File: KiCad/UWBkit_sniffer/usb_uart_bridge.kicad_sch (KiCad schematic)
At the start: 0 parts

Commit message: Added components to schematic
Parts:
- added C11: 100n, Capacitor_SMD:C_0603_1608Metric, symbol Device:C_Small
- added C12: 1u, Capacitor_Tantalum_SMD:CP_EIA-3216-18_Kemet-A, symbol Device:C_Polarized_Small
- added D6: G, LED_SMD:LED_0603_1608Metric, symbol Device:LED_Small
- added D7: R, LED_SMD:LED_0603_1608Metric, symbol Device:LED_Small
- added R10: 24k, Resistor_SMD:R_0603_1608Metric, symbol Device:R_Small
- added R11: 47k, Resistor_SMD:R_0603_1608Metric, symbol Device:R_Small
- added R13: 2k1, Resistor_SMD:R_0603_1608Metric, symbol Device:R_Small
- added R14: 3k3, Resistor_SMD:R_0603_1608Metric, symbol Device:R_Small
- added U2: CP2104, Package_DFN_QFN:QFN-24-1EP_4x4mm_P0.5mm_EP2.6x2.6mm, symbol Interface_USB:CP2104
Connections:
- new net: R10.2, R11.1, U2.8 (VBUS)
- new net: D6.1 (K), R13.1
- new net: R13.2, U2.13 (RXT/GPIO.1)
- new net: R14.1, U2.14 (TXT/GPIO.0)
- new net: D7.1 (K), R14.2
- new net +3V3: C11.1, C12.1, D6.2 (A), D7.2 (A), U2.5 (VIO), U2.6 (VDD), U2.7 (REGIN)
- new net D+: U2.3 (D+)
- new net D-: U2.4 (D-)
- new net GND: C11.2, C12.2, R11.2, U2.2 (GND), U2.25 (GND)
- new net RXD: U2.20 (RXD)
- new net TXD: U2.21 (TXD)
- new net VBUS: R10.1
- new net nRST: U2.9 (~{RST})
- no-connect marks 0 -> 11
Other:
- note added: "RX LED"
- note added: "TX LED"

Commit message: First version of PCB
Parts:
- added J11: Conn_01x02, Connector_PinHeader_2.54mm:PinHeader_1x02_P2.54mm_Vertical, symbol Connector_Generic:Conn_01x02
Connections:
- net RXD: now also J11.2 (Pin_2)
- net TXD: now also J11.1 (Pin_1)
- net at U2.14 (TXT/GPIO.0): now also R14.2; no longer R14.1
- net at D7.1 (K): now also R14.1; no longer R14.2
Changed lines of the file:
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@@
+	)
+	(junction
+		(at 166.37 72.39)
+		(diameter 0)
+		(color 0 0 0 0)
 	)
 	(junction
@@
 		(color 0 0 0 0)
 	)
+	(junction
+		(at 166.37 69.85)
+		(diameter 0)
+		(color 0 0 0 0)
+	)
 	(no_connect
 		(at 161.29 80.01)
@@
 	(wire
 		(pts
+			(xy 172.72 76.2) (xy 166.37 76.2)
+		)
+		(stroke
+			(width 0)
+			(type default)
+		)
+	)
+	(wire
+		(pts
+			(xy 166.37 72.39) (xy 168.91 72.39)
+		)
+		(stroke
+			(width 0)
+			(type default)
+		)
+	)
+	(wire
+		(pts
 			(xy 146.05 62.23) (xy 148.59 62.23)
 		)
@@
 	(wire
 		(pts
+			(xy 172.72 66.04) (xy 166.37 66.04)
+		)
+		(stroke
+			(width 0)
+			(type default)
+		)
+	)
+	(wire
+		(pts
 			(xy 102.87 69.85) (xy 102.87 71.12)
 		)
@@
 	(wire
 		(pts
-			(xy 161.29 69.85) (xy 163.83 69.85)
+			(xy 161.29 69.85) (xy 166.37 69.85)
 		)
 		(stroke
@@
 	(wire
 		(pts
+			(xy 166.37 69.85) (xy 168.91 69.85)
+		)
+		(stroke
+			(width 0)
+			(type default)
+		)
+	)
+	(wire
+		(pts
 			(xy 105.41 68.58) (xy 105.41 69.85)
 		)
@@
 	(wire
 		(pts
+			(xy 166.37 76.2) (xy 166.37 72.39)
+		)
+		(stroke
+			(width 0)
+			(type default)
+		)
+	)
+	(wire
+		(pts
 			(xy 173.99 106.68) (xy 172.72 106.68)
 		)
@@
 	(wire
 		(pts
-			(xy 161.29 72.39) (xy 163.83 72.39)
+			(xy 166.37 66.04) (xy 166.37 69.85)
+		)
+		(stroke
+			(width 0)
+			(type default)
+		)
+	)
+	(wire
+		(pts
+			(xy 161.29 72.39) (xy 166.37 72.39)
 		)
 		(stroke
@@
 		)
 	)
+	(hierarchical_label "RXD"
+		(shape input)
+		(at 172.72 76.2 0)
+		(effects
+			(font
+				(size 1.27 1.27)
+			)
+			(justify left)
+		)
+	)
 	(hierarchical_label "VBUS"
 		(shape input)
@@
 		)
 	)
-	(hierarchical_label "RXD"
-		(shape input)
-		(at 163.83 72.39 0)
-		(effects
-			(font
-				(size 1.27 1.27)
-			)
-			(justify left)
-		)
-	)
 	(hierarchical_label "nRST"
 		(shape input)
@@
 	(hierarchical_label "TXD"
 		(shape output)
-		(at 163.83 69.85 0)
+		(at 172.72 66.04 0)
 		(effects
 			(font
@@
 	)
 	(symbol
-		(lib_id "Device:R_Small")
-		(at 170.18 96.52 90)
-		(mirror x)
-		(unit 1)
-		(exclude_from_sim no)
-		(in_bom yes)
-		(on_board yes)
-		(dnp no)
-		(fields_autoplaced yes)
-		(property "Reference" "R14"
-			(at 170.18 91.44 90)
-			(effects
-				(font
-					(size 1.27 1.27)
-				)
-			)
-		)
-		(property "Value" "3k3"
-			(at 170.18 93.98 90)
-			(effects
-				(font
-					(size 1.27 1.27)
-				)
-			)
-		)
-		(property "Footprint" "Resistor_SMD:R_0603_1608Metric"
-			(at 170.18 96.52 0)
-			(effects
-				(font
-					(size 1.27 1.27)
-				)
-				(hide yes)
-			)
-		)
-		(property "Datasheet" "~"
-			(at 170.18 96.52 0)
-			(effects
-				(font
-					(size 1.27 1.27)
-				)
-				(hide yes)
-			)
-		)
-		(property "Description" "Resistor, small symbol"
-			(at 170.18 96.52 0)
-			(effects
-				(font
-					(size 1.27 1.27)
-				)
-				(hide yes)
-			)
-		)
-		(pin "1"
-		)
-		(pin "2"
-		)
-		(instances
-			(project "UWBkit_sniffer"
-				(path "/7666dc1a-7b28-48ea-a5e3-eea89f700cea/69acd281-5c2d-45c7-b47b-523f2587d598"
-					(reference "R14")
-					(unit 1)
-				)
-			)
-		)
-	)
-	(symbol
 		(lib_id "Device:LED_Small")
 		(at 176.53 106.68 0)
@@
 					(unit 1)
 				)
+			)
+		)
+	)
+	(symbol
+		(lib_id "Connector_Generic:Conn_01x02")
+		(at 173.99 69.85 0)
+		(unit 1)
+		(exclude_from_sim no)
+		(in_bom yes)
+		(on_board yes)
+		(dnp no)
+		(fields_autoplaced yes)
+		(property "Reference" "J11"
+			(at 176.53 69.8499 0)
+			(effects
+				(font
+					(size 1.27 1.27)
+				)
+				(justify left)
+			)
+		)
+		(property "Value" "Conn_01x02"
+			(at 176.53 72.3899 0)
+			(effects
+				(font
+					(size 1.27 1.27)
+				)
+				(justify left)
+			)
+		)
+		(property "Footprint" "Connector_PinHeader_2.54mm:PinHeader_1x02_P2.54mm_Vertical"
+			(at 173.99 69.85 0)
+			(effects
+				(font
+					(size 1.27 1.27)
+				)
+				(hide yes)
+			)
+		)
+		(property "Datasheet" "~"
+			(at 173.99 69.85 0)
+			(effects
+				(font
+					(size 1.27 1.27)
+				)
+				(hide yes)
+			)
+		)
+		(property "Description" "Generic connector, single row, 01x02, script generated (kicad-library-utils/schlib/autogen/connector/)"
+			(at 173.99 69.85 0)
+			(effects
+				(font
+					(size 1.27 1.27)
+				)
+				(hide yes)
+			)
+		)
+		(pin "2"
+		)
+		(pin "1"
+		)
+		(instances
+			(project ""
+				(path "/7666dc1a-7b28-48ea-a5e3-eea89f700cea/69acd281-5c2d-45c7-b47b-523f2587d598"
+					(reference "J11")
+					(unit 1)
+				)
+			)
+		)
+	)
+	(symbol
+		(lib_id "Device:R_Small")
+		(at 170.18 96.52 270)
+		(mirror x)
+		(unit 1)
+		(exclude_from_sim no)
+		(in_bom yes)
+		(on_board yes)
+		(dnp no)
+		(fields_autoplaced yes)
+		(property "Reference" "R14"
+			(at 170.18 91.44 90)
+			(effects
+				(font
+					(size 1.27 1.27)
+				)
+			)
+		)
+		(property "Value" "3k3"
+			(at 170.18 93.98 90)
+			(effects
+				(font
+					(size 1.27 1.27)
+				)
+			)
+		)
+		(property "Footprint" "Resistor_SMD:R_0603_1608Metric"
+			(at 170.18 96.52 0)
+			(effects
+				(font
+					(size 1.27 1.27)
+				)
+				(hide yes)
+			)
+		)
+		(property "Datasheet" "~"
+			(at 170.18 96.52 0)
+			(effects
+				(font
+					(size 1.27 1.27)
+				)
+				(hide yes)
+			)
+		)
+		(property "Description" "Resistor, small symbol"
+			(at 170.18 96.52 0)
+			(effects
+				(font
+					(size 1.27 1.27)
+				)
+				(hide yes)
+			)
+		)
+		(pin "1"
+		)
+		(pin "2"
+		)
+		(instances
+			(project "UWBkit_sniffer"
+				(path "/7666dc1a-7b28-48ea-a5e3-eea89f700cea/69acd281-5c2d-45c7-b47b-523f2587d598"
+					(reference "R14")
+					(unit 1)
+				)

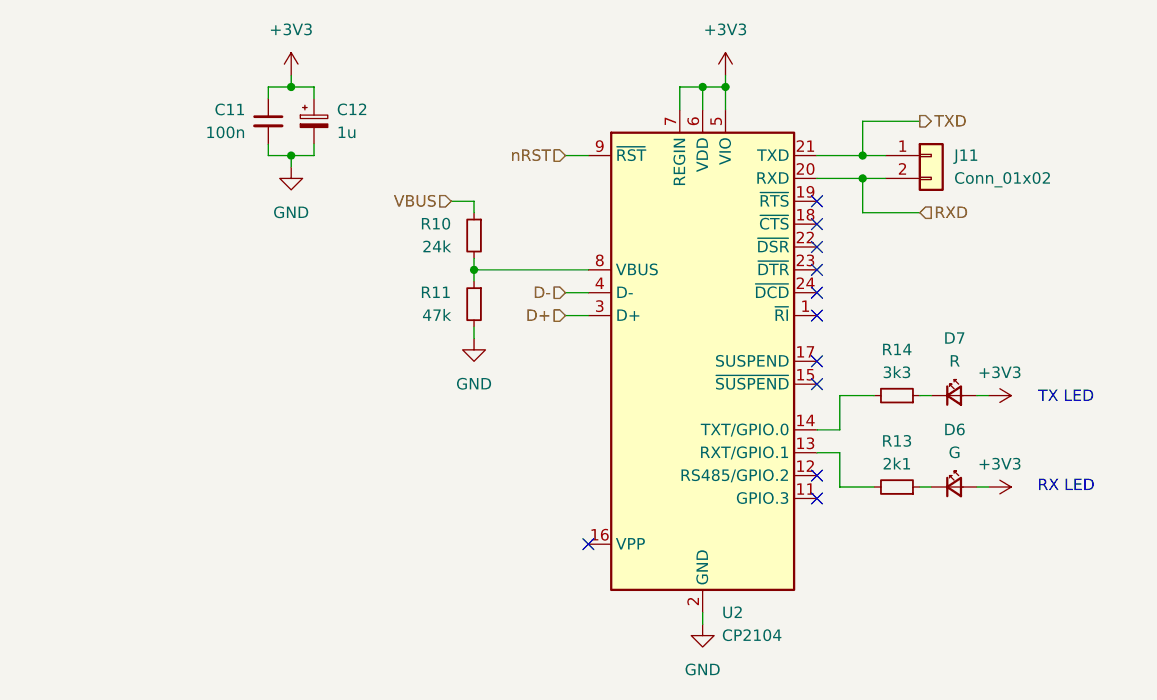
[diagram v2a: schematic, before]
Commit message: Added reset pullup for CP2014
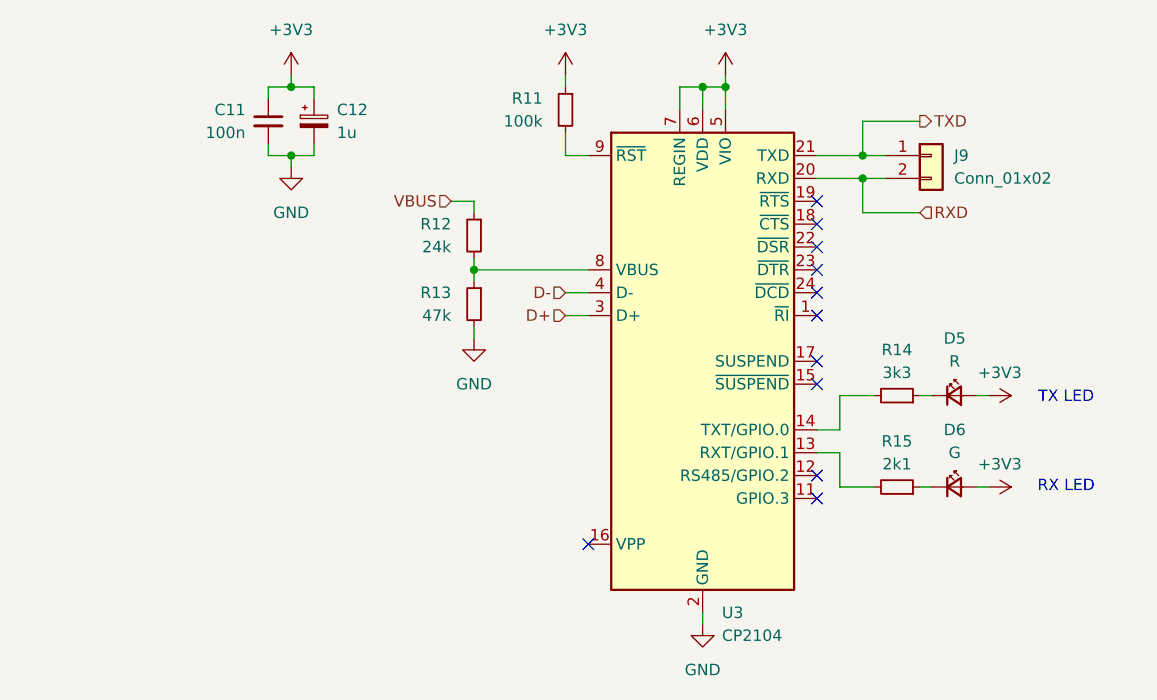
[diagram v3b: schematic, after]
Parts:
- added R11: 100k, Resistor_SMD:R_0603_1608Metric, symbol Device:R_Small
- renumbered D7 to D5, J11 to J9, R10 to R12, R11 to R13, R13 to R15, U2 to U3
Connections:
- net +3V3: now also R11.1
- net nRST: no longer names the net of U3.9 (~{RST})
- net nRST: now also R11.2
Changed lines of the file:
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@@
+	(wire
+		(pts
+			(xy 133.35 67.31) (xy 133.35 69.85)
+		)
+		(stroke
+			(width 0)
+			(type default)
+		)
+	)
+	(wire
+		(pts
+			(xy 133.35 60.96) (xy 133.35 62.23)
+		)
+		(stroke
+			(width 0)
+			(type default)
+		)
+	)
 	(wire
 		(pts
@@
 	(wire
 		(pts
+			(xy 133.35 69.85) (xy 135.89 69.85)
+		)
+		(stroke
+			(width 0)
+			(type default)
+		)
+	)
+	(wire
+		(pts
 			(xy 151.13 60.96) (xy 151.13 62.23)
 		)
@@
 		(pts
 			(xy 102.87 62.23) (xy 100.33 62.23)
-		)
-		(stroke
-			(width 0)
-			(type default)
-		)
-	)
-	(wire
-		(pts
-			(xy 133.35 69.85) (xy 135.89 69.85)
 		)
 		(stroke
@@
 		)
 	)
-	(hierarchical_label "nRST"
-		(shape input)
-		(at 133.35 69.85 180)
-		(effects
-			(font
-				(size 1.27 1.27)
-			)
-			(justify right)
-		)
-	)
 	(hierarchical_label "TXD"
 		(shape output)
@@
 		(on_board yes)
 		(dnp no)
-		(property "Reference" "R11"
+		(property "Reference" "R13"
 			(at 120.65 85.0899 0)
 			(effects
@@
 			(project "UWBkit_sniffer"
 				(path "/7666dc1a-7b28-48ea-a5e3-eea89f700cea/69acd281-5c2d-45c7-b47b-523f2587d598"
-					(reference "R11")
+					(reference "R13")
 					(unit 1)
 				)
@@
 		(dnp no)
 		(fields_autoplaced yes)
-		(property "Reference" "#PWR063"
+		(property "Reference" "#PWR057"
 			(at 176.53 106.68 0)
 			(effects
@@
 			(project "UWBkit_sniffer"
 				(path "/7666dc1a-7b28-48ea-a5e3-eea89f700cea/69acd281-5c2d-45c7-b47b-523f2587d598"
-					(reference "#PWR063")
+					(reference "#PWR057")
 					(unit 1)
 				)
@@
 		(dnp no)
 		(fields_autoplaced yes)
-		(property "Reference" "R13"
+		(property "Reference" "R15"
 			(at 170.18 101.6 90)
 			(effects
@@
 			(project "UWBkit_sniffer"
 				(path "/7666dc1a-7b28-48ea-a5e3-eea89f700cea/69acd281-5c2d-45c7-b47b-523f2587d598"
-					(reference "R13")
+					(reference "R15")
 					(unit 1)
 				)
@@
 		(on_board yes)
 		(dnp no)
-		(property "Reference" "R10"
+		(property "Reference" "R12"
 			(at 120.65 77.4699 0)
 			(effects
@@
 			(project "UWBkit_sniffer"
 				(path "/7666dc1a-7b28-48ea-a5e3-eea89f700cea/69acd281-5c2d-45c7-b47b-523f2587d598"
-					(reference "R10")
+					(reference "R12")
 					(unit 1)
 				)
@@
 		(dnp no)
 		(fields_autoplaced yes)
-		(property "Reference" "#PWR061"
+		(property "Reference" "#PWR055"
 			(at 123.19 96.52 0)
 			(effects
@@
 			(project "UWBkit_sniffer"
 				(path "/7666dc1a-7b28-48ea-a5e3-eea89f700cea/69acd281-5c2d-45c7-b47b-523f2587d598"
-					(reference "#PWR061")
+					(reference "#PWR055")
 					(unit 1)
 				)
@@
 		(dnp no)
 		(fields_autoplaced yes)
-		(property "Reference" "U2"
+		(property "Reference" "U3"
 			(at 150.7333 120.65 0)
 			(effects
@@
 			(project ""
 				(path "/7666dc1a-7b28-48ea-a5e3-eea89f700cea/69acd281-5c2d-45c7-b47b-523f2587d598"
-					(reference "U2")
+					(reference "U3")
 					(unit 1)
 				)
@@
 		(dnp no)
 		(fields_autoplaced yes)
-		(property "Reference" "#PWR060"
+		(property "Reference" "#PWR054"
 			(at 102.87 77.47 0)
 			(effects
@@
 			(project "UWBkit_sniffer"
 				(path "/7666dc1a-7b28-48ea-a5e3-eea89f700cea/69acd281-5c2d-45c7-b47b-523f2587d598"
-					(reference "#PWR060")
+					(reference "#PWR054")
 					(unit 1)
 				)
@@
 		(dnp no)
 		(fields_autoplaced yes)
-		(property "Reference" "#PWR056"
+		(property "Reference" "#PWR058"
 			(at 148.59 128.27 0)
 			(effects
@@
 			(project ""
 				(path "/7666dc1a-7b28-48ea-a5e3-eea89f700cea/69acd281-5c2d-45c7-b47b-523f2587d598"
-					(reference "#PWR056")
+					(reference "#PWR058")
 					(unit 1)
 				)
@@
 		(dnp no)
 		(fields_autoplaced yes)
-		(property "Reference" "J11"
+		(property "Reference" "J9"
 			(at 176.53 69.8499 0)
 			(effects
@@
 			(project ""
 				(path "/7666dc1a-7b28-48ea-a5e3-eea89f700cea/69acd281-5c2d-45c7-b47b-523f2587d598"
-					(reference "J11")
+					(reference "J9")
 					(unit 1)
 				)
@@
 		(dnp no)
 		(fields_autoplaced yes)
-		(property "Reference" "#PWR064"
+		(property "Reference" "#PWR056"
 			(at 176.53 96.52 0)
 			(effects
@@
 			(project "UWBkit_sniffer"
 				(path "/7666dc1a-7b28-48ea-a5e3-eea89f700cea/69acd281-5c2d-45c7-b47b-523f2587d598"
-					(reference "#PWR064")
+					(reference "#PWR056")
+					(unit 1)
+				)
+			)
+		)
+	)
+	(symbol
+		(lib_id "Device:R_Small")
+		(at 133.35 64.77 0)
+		(mirror y)
+		(unit 1)
+		(exclude_from_sim no)
+		(in_bom yes)
+		(on_board yes)
+		(dnp no)
+		(property "Reference" "R11"
+			(at 130.81 63.4999 0)
+			(effects
+				(font
+					(size 1.27 1.27)
+				)
+				(justify left)
+			)
+		)
+		(property "Value" "100k"
+			(at 130.81 66.0399 0)
+			(effects
+				(font
+					(size 1.27 1.27)
+				)
+				(justify left)
+			)
+		)
+		(property "Footprint" "Resistor_SMD:R_0603_1608Metric"
+			(at 133.35 64.77 0)
+			(effects
+				(font
+					(size 1.27 1.27)
+				)
+				(hide yes)
+			)
+		)
+		(property "Datasheet" "~"
+			(at 133.35 64.77 0)
+			(effects
+				(font
+					(size 1.27 1.27)
+				)
+				(hide yes)
+			)
+		)
+		(property "Description" "Resistor, small symbol"
+			(at 133.35 64.77 0)
+			(effects
+				(font
+					(size 1.27 1.27)
+				)
+				(hide yes)
+			)
+		)
+		(pin "1"
+		)
+		(pin "2"
+		)
+		(instances
+			(project "UWBkit_sniffer"
+				(path "/7666dc1a-7b28-48ea-a5e3-eea89f700cea/69acd281-5c2d-45c7-b47b-523f2587d598"
+					(reference "R11")
 					(unit 1)
 				)
@@
 		(dnp no)
 		(fields_autoplaced yes)
-		(property "Reference" "#PWR059"
+		(property "Reference" "#PWR051"
 			(at 102.87 64.77 0)
 			(effects
@@
 			(project "UWBkit_sniffer"
 				(path "/7666dc1a-7b28-48ea-a5e3-eea89f700cea/69acd281-5c2d-45c7-b47b-523f2587d598"
-					(reference "#PWR059")
+					(reference "#PWR051")
+					(unit 1)
+				)
+			)
+		)
+	)
+	(symbol
+		(lib_id "power:+3V3")
+		(at 133.35 60.96 0)
+		(unit 1)
+		(exclude_from_sim no)
+		(in_bom yes)
+		(on_board yes)
+		(dnp no)
+		(fields_autoplaced yes)
+		(property "Reference" "#PWR052"
+			(at 133.35 64.77 0)
+			(effects
+				(font
+					(size 1.27 1.27)
+				)
+				(hide yes)
+			)
+		)
+		(property "Value" "+3V3"
+			(at 133.35 55.88 0)
+			(effects
+				(font
+					(size 1.27 1.27)
+				)
+			)
+		)
+		(property "Footprint" ""
+			(at 133.35 60.96 0)
+			(effects
+				(font
+					(size 1.27 1.27)
+				)
+				(hide yes)
+			)
+		)
+		(property "Datasheet" ""
+			(at 133.35 60.96 0)
+			(effects
+				(font
+					(size 1.27 1.27)
+				)
+				(hide yes)
+			)
+		)
+		(property "Description" "Power symbol creates a global label with name \"+3V3\""
+			(at 133.35 60.96 0)
+			(effects
+				(font
+					(size 1.27 1.27)
+				)
+				(hide yes)
+			)
+		)
+		(pin "1"
+		)
+		(instances
+			(project "UWBkit_sniffer"
+				(path "/7666dc1a-7b28-48ea-a5e3-eea89f700cea/69acd281-5c2d-45c7-b47b-523f2587d598"
+					(reference "#PWR052")
 					(unit 1)
 				)
@@
 		(dnp no)
 		(fields_autoplaced yes)
-		(property "Reference" "D7"
+		(property "Reference" "D5"
 			(at 176.5935 90.17 0)
 			(effects
@@
 			(project "UWBkit_sniffer"
 				(path "/7666dc1a-7b28-48ea-a5e3-eea89f700cea/69acd281-5c2d-45c7-b47b-523f2587d598"
-					(reference "D7")
+					(reference "D5")
 					(unit 1)
 				)
@@
 		(dnp no)
 		(fields_autoplaced yes)
-		(property "Reference" "#PWR058"
+		(property "Reference" "#PWR053"
 			(at 151.13 64.77 0)
 			(effects
@@
 			(project ""
 				(path "/7666dc1a-7b28-48ea-a5e3-eea89f700cea/69acd281-5c2d-45c7-b47b-523f2587d598"
-					(reference "#PWR058")
-					(unit 1)
-				)
+					(reference "#PWR053")
+					(unit 1)
+				)

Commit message: Removed UWA.01, added CTS/RTS connections
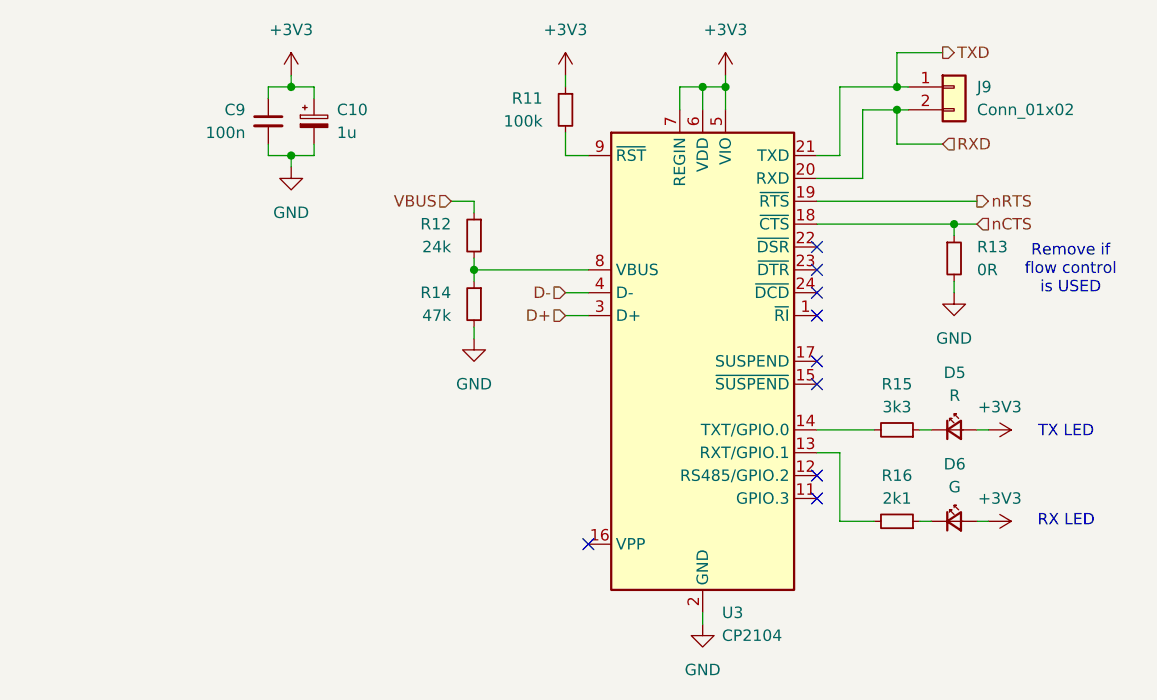
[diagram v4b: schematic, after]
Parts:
- added R13: 0R, Resistor_SMD:R_0603_1608Metric, symbol Device:R_Small
- renumbered C12 to C10, C11 to C9, R13 to R14, R14 to R15, R15 to R16
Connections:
- net GND: now also R13.2
- net nCTS: now reaches U3.18 (~{CTS})
- net nCTS: now also R13.1
- net nRTS: now reaches U3.19 (~{RTS})
- no-connect marks 11 -> 9
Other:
- note added: "Remove if flow control is USED"
- moved on the sheet: D5, D6, J9, R15, R16

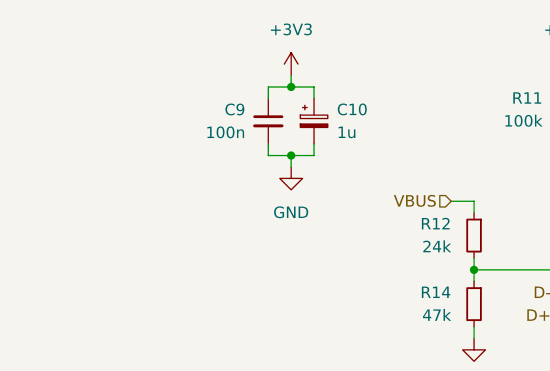
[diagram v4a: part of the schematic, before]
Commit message: Improved placement of ICs and ports and the board is now smaller
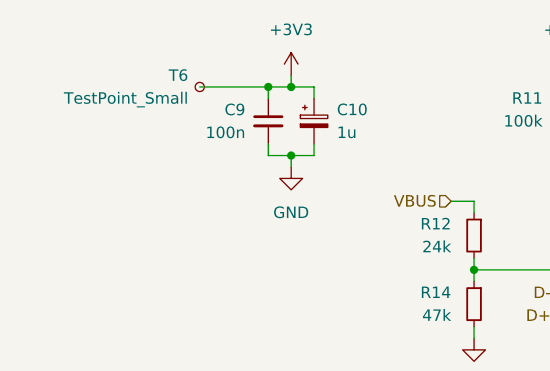
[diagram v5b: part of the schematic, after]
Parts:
- added T6: TestPoint_Small, TestPoint:TestPoint_Pad_D1.0mm, symbol Connector:TestPoint_Small
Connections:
- net +3V3: now also T6.1
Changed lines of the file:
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@@
+	)
+	(junction
+		(at 100.33 62.23)
+		(diameter 0)
+		(color 0 0 0 0)
 	)
 	(junction
@@
 		(pts
 			(xy 161.29 77.47) (xy 176.53 77.47)
+		)
+		(stroke
+			(width 0)
+			(type default)
+		)
+	)
+	(wire
+		(pts
+			(xy 92.71 62.23) (xy 100.33 62.23)
 		)
 		(stroke
@@
 					(unit 1)
 				)
+			)
+		)
+	)
+	(symbol
+		(lib_id "Connector:TestPoint_Small")
+		(at 92.71 62.23 0)
+		(mirror y)
+		(unit 1)
+		(exclude_from_sim no)
+		(in_bom no)
+		(on_board yes)
+		(dnp no)
+		(property "Reference" "T6"
+			(at 91.44 60.9599 0)
+			(effects
+				(font
+					(size 1.27 1.27)
+				)
+				(justify left)
+			)
+		)
+		(property "Value" "TestPoint_Small"
+			(at 91.44 63.4999 0)
+			(effects
+				(font
+					(size 1.27 1.27)
+				)
+				(justify left)
+			)
+		)
+		(property "Footprint" "TestPoint:TestPoint_Pad_D1.0mm"
+			(at 87.63 62.23 0)
+			(effects
+				(font
+					(size 1.27 1.27)
+				)
+				(hide yes)
+			)
+		)
+		(property "Datasheet" "~"
+			(at 87.63 62.23 0)
+			(effects
+				(font
+					(size 1.27 1.27)
+				)
+				(hide yes)
+			)
+		)
+		(property "Description" "test point"
+			(at 92.71 62.23 0)
+			(effects
+				(font
+					(size 1.27 1.27)
+				)
+				(hide yes)
+			)
+		)
+		(pin "1"
+		)
+		(instances
+			(project "UWBkit_sniffer"
+				(path "/7666dc1a-7b28-48ea-a5e3-eea89f700cea/69acd281-5c2d-45c7-b47b-523f2587d598"
+					(reference "T6")
+					(unit 1)
+				)

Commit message: Release V1.0
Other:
- title: (none) -> USB to UART Bridge
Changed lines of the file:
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@@
 	(generator_version "9.0")
 	(paper "A4")
+	(title_block
+		(title "USB to UART Bridge")
+		(date "2026-02-24")
+		(rev "1.0")
+	)
 	(text "Remove if\nflow control\nis USED"
 		(exclude_from_sim no)
